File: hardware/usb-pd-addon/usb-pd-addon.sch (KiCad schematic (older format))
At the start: 13 parts, among them J1 Conn_02x10_Odd_Even, J2 Conn_02x10_Odd_Even, J3 USB_TYPE_C, U1 FUSB302B, U2 AP2171W, U3 SN74AVC1T45DBVR, U4 SN74AVC1T45DBVR, U5 SN74AVC1T45DBVR, U6 SN74AVC1T45DBVR

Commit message: v0.2a: Added adjustable LDOs for the level shifter reference voltages for USB and SBU pairs.
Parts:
- added J4, J5: Conn_02x05_Odd_Even, Connector_PinHeader_2.54mm:PinHeader_2x05_P2.54mm_Vertical, symbol Connector_Generic:Conn_02x05_Odd_Even
- added R10, R9: 4.7k, pkl_dipol:R_0603, symbol pkl_device:pkl_R_Small
- added R11, R13: 1.2k, pkl_dipol:R_0603, symbol pkl_device:pkl_R_Small
- added R12, R14: 6.8k, pkl_dipol:R_0603, symbol pkl_device:pkl_R_Small
- added R15, R16: 12k, pkl_dipol:R_0603, symbol pkl_device:pkl_R_Small
- added R17, R18: 20k, pkl_dipol:R_0603, symbol pkl_device:pkl_R_Small
- added R5, R6: 10k, pkl_dipol:R_0603, symbol pkl_device:pkl_R_Small
- added R7, R8: 3.3k, pkl_dipol:R_0603, symbol pkl_device:pkl_R_Small
- added U7, U8: AP2127K-ADJ, Package_TO_SOT_SMD:SOT-23-5, symbol Regulator_Linear:AP2127K-ADJ
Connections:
- net labels added: 1V2_SBU, 1V2_USB, 1V5_SBU, 1V5_USB, 1V8_SBU, 1V8_USB, 2V5_SBU, 2V5_USB, 3V3_SBU, 3V3_USB
- wire segments 118 -> 188
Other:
- moved on the sheet: R4, U2

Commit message: Updated USB-C symbol, no functional change.
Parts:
- J3: symbol pkl_conn:USB_TYPE_C -> Connector:USB_C_Receptacle_USB2.0
- R1, R2, R3: value 1K -> 2K2; LCSC C21190 -> C4190
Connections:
- wire segments 188 -> 182
- no-connect marks 17 -> 9
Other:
- moved on the sheet: R1
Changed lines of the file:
@@
 Wire Wire Line
 	6450 1600 6450 1500
-Wire Wire Line
-	10350 2150 10450 2150
-Text Label 10450 2150 0    50   ~ 0
-VBUS
-Text Label 8500 1750 2    50   ~ 0
+Text Label 10200 1500 0    50   ~ 0
 CC1
-Text Label 10450 2050 0    50   ~ 0
+Text Label 10200 1600 0    50   ~ 0
 CC2
-Text Label 8500 1950 2    50   ~ 0
+Text Label 10250 1800 0    50   ~ 0
 USBN
-Text Label 10450 1850 0    50   ~ 0
-USBN
-Text Label 8500 1850 2    50   ~ 0
+Text Label 10250 2000 0    50   ~ 0
 USBP
-Text Label 10450 1950 0    50   ~ 0
-USBP
-Text Label 8500 2050 2    50   ~ 0
+Text Label 10200 2400 0    50   ~ 0
 SBU1
-Text Label 10450 1750 0    50   ~ 0
+Text Label 10200 2500 0    50   ~ 0
 SBU2
 $Comp
-L pkl_conn:USB_TYPE_C J3
+L Connector:USB_C_Receptacle_USB2.0 J3
 U 1 1 6025891B
 P 9500 1900
@@
 F 1 "USB_TYPE_C" H 9475 2681 60  0000 C CNN
 F 2 "pkl_connectors:USB_C_Receptacle_HRO_TYPE-C-31-M-12" H 9550 600 60  0001 C CNN
-F 3 "" H 9500 1900 60  0001 C CNN
+F 3 "https://www.usb.org/sites/default/files/documents/usb_type-c.zip" H 9500 1900 60  0001 C CNN
 F 4 "C165948" H 9500 500 50  0001 C CNN "LCSC"
 	1    9500 1900
@@
 $EndComp
 Wire Wire Line
-	8600 2150 8500 2150
-Wire Wire Line
-	8600 1650 8500 1650
-Wire Wire Line
-	8450 2450 8600 2450
-Wire Wire Line
-	8450 1350 8600 1350
-Text Label 8500 1650 2    50   ~ 0
-VBUS
-Text Label 8500 2150 2    50   ~ 0
-VBUS
-Wire Wire Line
-	10350 1650 10450 1650
-Wire Wire Line
-	10350 1350 10500 1350
-Wire Wire Line
-	10350 2450 10500 2450
-Wire Wire Line
-	9500 2800 9500 2900
+	10100 1300 10200 1300
 $Comp
 L power:GND #PWR017
 U 1 1 60290841
-P 9500 2800
-F 0 "#PWR017" H 9500 2550 50  0001 C CNN
-F 1 "GND" H 9505 2627 50  0000 C CNN
-F 2 "" H 9500 2800 50  0001 C CNN
-F 3 "" H 9500 2800 50  0001 C CNN
-	1    9500 2800
-	1    0    0    -1
-$EndComp
-Text Label 10450 1650 0    50   ~ 0
+P 9500 2900
+F 0 "#PWR017" H 9500 2650 50  0001 C CNN
+F 1 "GND" H 9505 2727 50  0000 C CNN
+F 2 "" H 9500 2900 50  0001 C CNN
+F 3 "" H 9500 2900 50  0001 C CNN
+	1    9500 2900
+	1    0    0    -1
+$EndComp
+Text Label 10200 1300 0    50   ~ 0
 VBUS
 Wire Wire Line
-	8500 1750 8600 1750
-Wire Wire Line
-	8500 1850 8600 1850
-Wire Wire Line
-	8500 1950 8600 1950
-Wire Wire Line
-	8500 2050 8600 2050
-NoConn ~ 10350 1450
-NoConn ~ 10350 1550
-NoConn ~ 10350 2250
-NoConn ~ 10350 2350
-NoConn ~ 8600 2350
-NoConn ~ 8600 2250
-NoConn ~ 8600 1550
-NoConn ~ 8600 1450
-Wire Wire Line
-	10350 1750 10450 1750
-Wire Wire Line
-	10350 1850 10450 1850
-Wire Wire Line
-	10350 1950 10450 1950
-Wire Wire Line
-	10350 2050 10450 2050
+	10100 2500 10200 2500
 $Comp
 L power:+5V #PWR013
@@
 Connection ~ 6650 1500
 $Comp
-L pkl_device:pkl_R R3
-U 1 1 6044137D
-P 5650 1650
-F 0 "R3" H 5580 1604 50  0000 R CNN
-F 1 "1K" H 5580 1695 50  0000 R CNN
-F 2 "pkl_dipol:R_0603" V 5580 1650 30  0001 C CNN
-F 3 "" H 5650 1650 30  0000 C CNN
-F 4 "C21190" H 5650 1650 50  0001 C CNN "LCSC"
-	1    5650 1650
-	-1   0    0    1
-$EndComp
-$Comp
-L pkl_device:pkl_R R2
-U 1 1 60442B4F
-P 5400 1650
-F 0 "R2" H 5330 1604 50  0000 R CNN
-F 1 "1K" H 5330 1695 50  0000 R CNN
-F 2 "pkl_dipol:R_0603" V 5330 1650 30  0001 C CNN
-F 3 "" H 5400 1650 30  0000 C CNN
-F 4 "C21190" H 5400 1650 50  0001 C CNN "LCSC"
-	1    5400 1650
-	-1   0    0    1
-$EndComp
-$Comp
 L pkl_device:pkl_R R1
 U 1 1 604439D3
-P 5150 1650
-F 0 "R1" H 5080 1604 50  0000 R CNN
-F 1 "1K" H 5080 1695 50  0000 R CNN
-F 2 "pkl_dipol:R_0603" V 5080 1650 30  0001 C CNN
-F 3 "" H 5150 1650 30  0000 C CNN
-F 4 "C21190" H 5150 1650 50  0001 C CNN "LCSC"
-	1    5150 1650
+P 5050 1650
+F 0 "R1" H 4980 1604 50  0000 R CNN
+F 1 "2K2" H 4980 1695 50  0000 R CNN
+F 2 "pkl_dipol:R_0603" V 4980 1650 30  0001 C CNN
+F 3 "" H 5050 1650 30  0000 C CNN
+F 4 "C4190" H 5050 1650 50  0001 C CNN "LCSC"
+	1    5050 1650
 	-1   0    0    1
 $EndComp
 Wire Wire Line
-	5400 2000 5400 1850
-Wire Wire Line
-	5400 2000 6050 2000
-Wire Wire Line
 	4050 1450 4350 1450
 Wire Wire Line
-	5150 1450 5400 1450
+	5050 1450 5350 1450
 $Comp
 L Power_Management:AP2171W U2
@@
 Text Label 3800 5150 0    50   ~ 0
 VIO_SBU
-Connection ~ 5400 1450
-Wire Wire Line
-	5400 1450 5650 1450
 Wire Wire Line
 	5650 2100 5650 1850
 Wire Wire Line
 	5650 2100 6050 2100
-Wire Wire Line
-	6050 1900 5150 1900
-Wire Wire Line
-	5150 1900 5150 1850
 $Comp
 L power:+5V #PWR0101
 U 1 1 6089F777
-P 5400 1450
-F 0 "#PWR0101" H 5400 1300 50  0001 C CNN
-F 1 "+5V" H 5415 1623 50  0000 C CNN
-F 2 "" H 5400 1450 50  0001 C CNN
-F 3 "" H 5400 1450 50  0001 C CNN
-	1    5400 1450
-	1    0    0    -1
-$EndComp
-$Comp
-L power:GND #PWR0102
-U 1 1 608FF2F5
-P 8450 1350
-F 0 "#PWR0102" H 8450 1100 50  0001 C CNN
-F 1 "GND" H 8455 1177 50  0000 C CNN
-F 2 "" H 8450 1350 50  0001 C CNN
-F 3 "" H 8450 1350 50  0001 C CNN
-	1    8450 1350
-	1    0    0    -1
-$EndComp
-$Comp
-L power:GND #PWR0103
-U 1 1 608FF6A6
-P 8450 2450
-F 0 "#PWR0103" H 8450 2200 50  0001 C CNN
-F 1 "GND" H 8455 2277 50  0000 C CNN
-F 2 "" H 8450 2450 50  0001 C CNN
-F 3 "" H 8450 2450 50  0001 C CNN
-	1    8450 2450
-	1    0    0    -1
-$EndComp
-$Comp
-L power:GND #PWR0104
-U 1 1 608FF9F7
-P 10500 2450
-F 0 "#PWR0104" H 10500 2200 50  0001 C CNN
-F 1 "GND" H 10505 2277 50  0000 C CNN
-F 2 "" H 10500 2450 50  0001 C CNN
-F 3 "" H 10500 2450 50  0001 C CNN
-	1    10500 2450
-	1    0    0    -1
-$EndComp
-$Comp
-L power:GND #PWR0105
-U 1 1 608FFC48
-P 10500 1350
-F 0 "#PWR0105" H 10500 1100 50  0001 C CNN
-F 1 "GND" H 10505 1177 50  0000 C CNN
-F 2 "" H 10500 1350 50  0001 C CNN
-F 3 "" H 10500 1350 50  0001 C CNN
-	1    10500 1350
+P 5350 1450
+F 0 "#PWR0101" H 5350 1300 50  0001 C CNN
+F 1 "+5V" H 5365 1623 50  0000 C CNN
+F 2 "" H 5350 1450 50  0001 C CNN
+F 3 "" H 5350 1450 50  0001 C CNN
+	1    5350 1450
 	1    0    0    -1
 $EndComp
@@
 NoConn ~ 3350 2050
 NoConn ~ 3350 2150
-Connection ~ 9500 2800
 Text Label 6250 4600 0    50   ~ 0
 1V2_USB
@@
 	1    0    0    -1
 $EndComp
+Wire Wire Line
+	10100 2400 10200 2400
+Wire Wire Line
+	10100 2100 10100 2000
+Wire Wire Line
+	10100 2000 10250 2000
+Connection ~ 10100 2000
+Wire Wire Line
+	10100 1900 10100 1800
+Wire Wire Line
+	10100 1800 10250 1800
+Connection ~ 10100 1800
+Wire Wire Line
+	10100 1600 10200 1600
+Wire Wire Line
+	10100 1500 10200 1500
+Wire Wire Line
+	9500 2800 9500 2900
+$Comp
+L power:GND #PWR010
+U 1 1 6032ABD7
+P 9200 2900
+F 0 "#PWR010" H 9200 2650 50  0001 C CNN
+F 1 "GND" H 9205 2727 50  0000 C CNN
+F 2 "" H 9200 2900 50  0001 C CNN
+F 3 "" H 9200 2900 50  0001 C CNN
+	1    9200 2900
+	1    0    0    -1
+$EndComp
+Wire Wire Line
+	9200 2800 9200 2900
+$Comp
+L pkl_device:pkl_R R2
+U 1 1 60275996
+P 5350 1650
+F 0 "R2" H 5280 1604 50  0000 R CNN
+F 1 "2K2" H 5280 1695 50  0000 R CNN
+F 2 "pkl_dipol:R_0603" V 5280 1650 30  0001 C CNN
+F 3 "" H 5350 1650 30  0000 C CNN
+F 4 "C4190" H 5350 1650 50  0001 C CNN "LCSC"
+	1    5350 1650
+	-1   0    0    1
+$EndComp
+$Comp
+L pkl_device:pkl_R R3
+U 1 1 60275C57
+P 5650 1650
+F 0 "R3" H 5580 1604 50  0000 R CNN
+F 1 "2K2" H 5580 1695 50  0000 R CNN
+F 2 "pkl_dipol:R_0603" V 5580 1650 30  0001 C CNN
+F 3 "" H 5650 1650 30  0000 C CNN
+F 4 "C4190" H 5650 1650 50  0001 C CNN "LCSC"
+	1    5650 1650
+	-1   0    0    1
+$EndComp
+Connection ~ 5350 1450
+Wire Wire Line
+	5350 1450 5650 1450
+Wire Wire Line
+	5050 1850 5050 1900
+Wire Wire Line
+	5050 1900 6050 1900
+Wire Wire Line
+	5350 1850 5350 2000
+Wire Wire Line
+	5350 2000 6050 2000
 $EndSCHEMATC

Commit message: Added more resistors to fine tune level shifter reference voltages.
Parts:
- removed R8: 3.3k, pkl_dipol:R_0603, symbol pkl_device:pkl_R_Small
- removed U4, U5, U6: SN74AVC1T45DBVR, Package_TO_SOT_SMD:SOT-363_SC-70-6, symbol Logic_LevelTranslator:SN74LVC1T45DCK
- added FID1, FID2: Fiducial, Fiducial:Fiducial_1mm_Mask2mm, symbol Mechanical:Fiducial
- added J6: EXT, Connector_PinHeader_2.54mm:PinHeader_1x02_P2.54mm_Vertical, symbol Connector_Generic:Conn_01x02
- added J7: TP1, Connector_PinHeader_2.54mm:PinHeader_1x02_P2.54mm_Vertical, symbol Connector_Generic:Conn_01x02
- added J8: TP2, Connector_PinHeader_2.54mm:PinHeader_1x02_P2.54mm_Vertical, symbol Connector_Generic:Conn_01x02
- added J9: TP3, Connector_PinHeader_2.54mm:PinHeader_1x02_P2.54mm_Vertical, symbol Connector_Generic:Conn_01x02
- added LOGO1, LOGO2: Logo_Open_Hardware_Small, Symbol:OSHW-Logo2_7.3x6mm_SilkScreen, symbol Graphic:Logo_Open_Hardware_Small
- added R11, R22: 1K2, pkl_dipol:R_0603, symbol pkl_device:pkl_R_Small
- added R13, R19, R24, R30: 0R, pkl_dipol:R_0603, symbol pkl_device:pkl_R_Small
- added R17, R28: 1K5, pkl_dipol:R_0603, symbol pkl_device:pkl_R_Small
- added R21: 2K0, pkl_dipol:R_0603, symbol pkl_device:pkl_R_Small
- added R4, R5, R6: 2K2, pkl_dipol:R_0603, symbol pkl_device:pkl_R
- added R7: 1K, pkl_dipol:R_0603, symbol pkl_device:pkl_R
- added TH1, TH2, TH3: Mounting_Hole, pkl_pads:ToolingHole, symbol Mechanical:MountingHole
- added U4, U5, U6: SN74AVC1T45DBVR, Package_TO_SOT_SMD:SOT-23-6, symbol Logic_LevelTranslator:SN74LVC1T45DBV
- R12: renamed from R7; value 3.3k -> 2K0; LCSC C22978 -> C22975
- R14: renamed from R9; value 4.7k -> 4K7
- R15: renamed from R11; value 1.2k -> 1K2
- R16: renamed from R12; value 6.8k -> 6K8
- R18: renamed from R15; value 12k -> 10K; LCSC C22790 -> C25804
- R20: renamed from R17; value 20k -> 20K
- R23: renamed from R10; value 4.7k -> 4K7
- R25: renamed from R14; value 6.8k -> 6K8
- R26: renamed from R13; value 1.2k -> 1K2
- R27: renamed from R16; value 12k -> 10K; LCSC C22790 -> C25804
- R29: renamed from R18; value 20k -> 20K
- U3: footprint Package_TO_SOT_SMD:SOT-363_SC-70-6 -> Package_TO_SOT_SMD:SOT-23-6; symbol Logic_LevelTranslator:SN74LVC1T45DCK -> Logic_LevelTranslator:SN74LVC1T45DBV
- U7, U8: LCSC (none) -> C96343
- renumbered R6 to R10, R4 to R8, R5 to R9
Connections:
- net labels added: A3, A4, A5, ADJ_SBU, ADJ_USB, FLT_N, VEN
- net labels removed: AS, FAULT_N, VBUS_EN
- wire segments 182 -> 189
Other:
- moved on the sheet: R15, R16, R25, R26

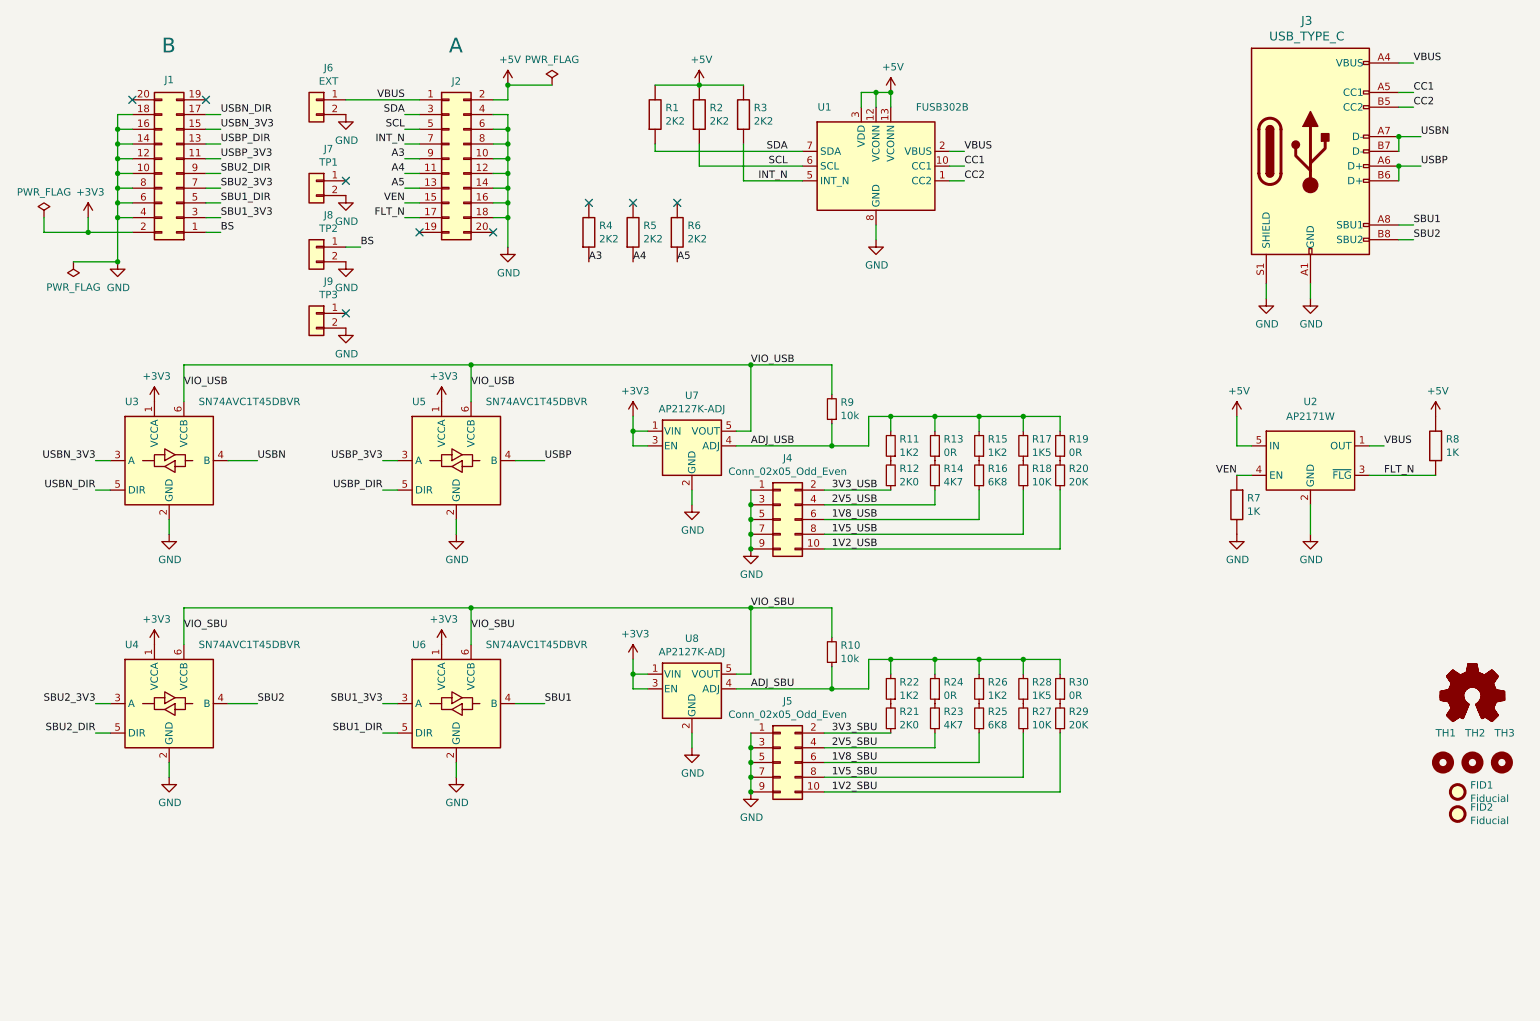
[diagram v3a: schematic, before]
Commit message: Added bypass caps.
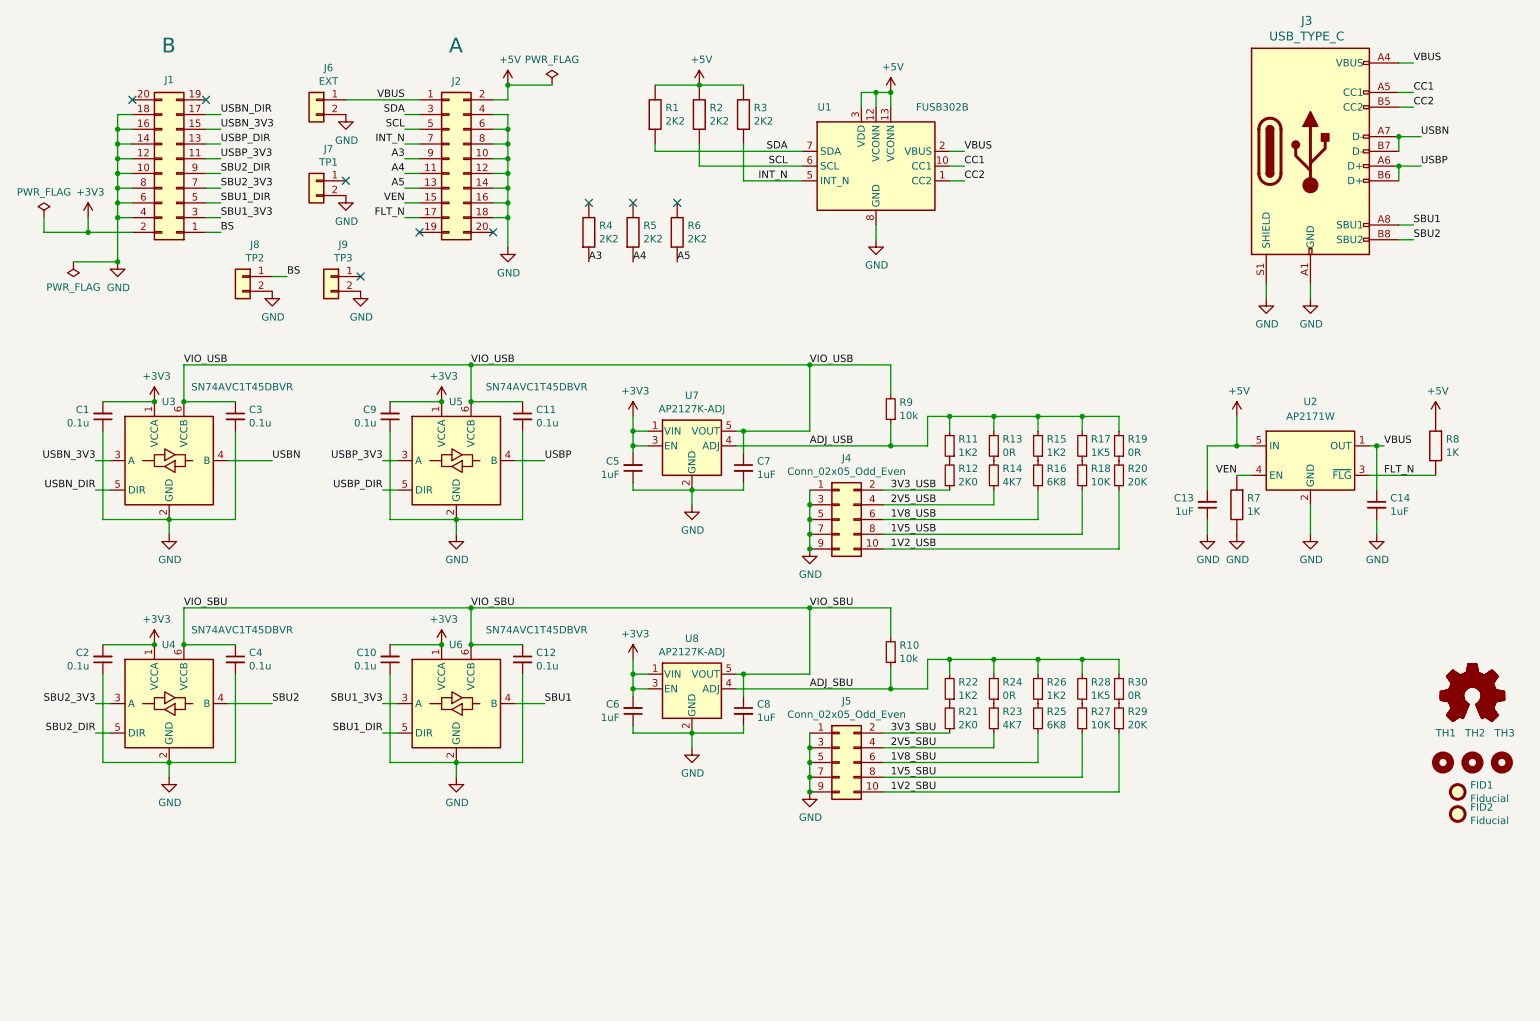
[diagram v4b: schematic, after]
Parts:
- added C1, C10, C11, C12, C2, C3, C4, C9: 0.1u, pkl_dipol:C_0603, symbol Device:C_Small
- added C13, C14, C5, C6, C7, C8: 1uF, pkl_dipol:C_0603, symbol Device:C_Small
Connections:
- net +3V3: now also C1.2, C10.2, C2.2, C5.2, C6.2, C9.2
- net +5V: now also C13.2
- net GND: now also C1.1, C10.1, C11.2, C12.2, C13.1, C14.2, C2.1, C3.2, C4.2, C5.1, C6.1, C7.2, C8.2, C9.1
- net VBUS: now also C14.1
- net VIO_SBU: now also C12.1, C4.1, C8.1
- net VIO_USB: now also C11.1, C3.1, C7.1
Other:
- moved on the sheet: J4, J5, J8, J9, R10, R11, R12, R13, R14, R15, R16, R17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
